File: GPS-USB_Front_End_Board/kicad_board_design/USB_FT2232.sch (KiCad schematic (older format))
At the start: 38 parts, among them J1 Micro-USB Connector, U1 93LCxxB, U2 FT2232HL-REEL, U3 L4931 LDO, Y1 12MHz Crystal

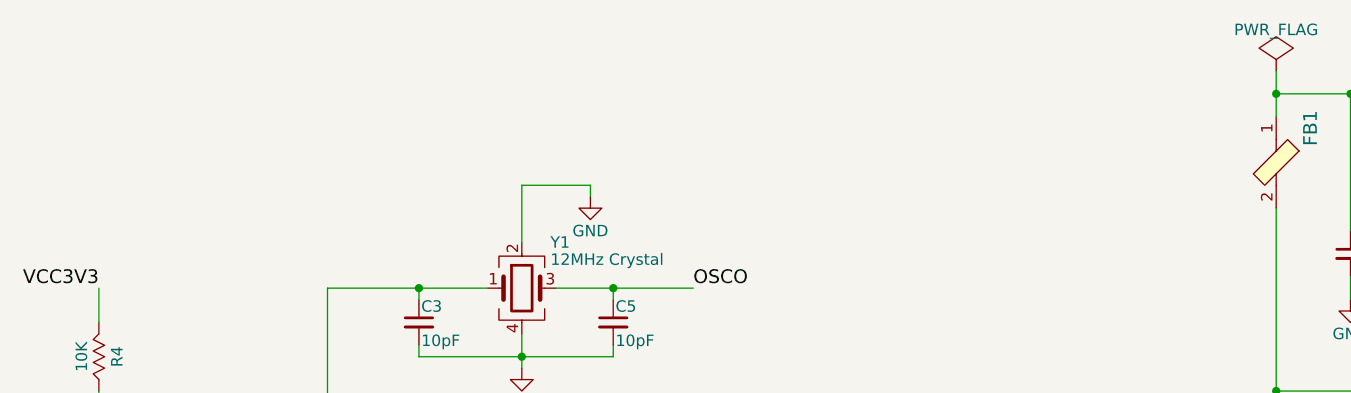
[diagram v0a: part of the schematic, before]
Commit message: Add more decoupling caps to 2232H.
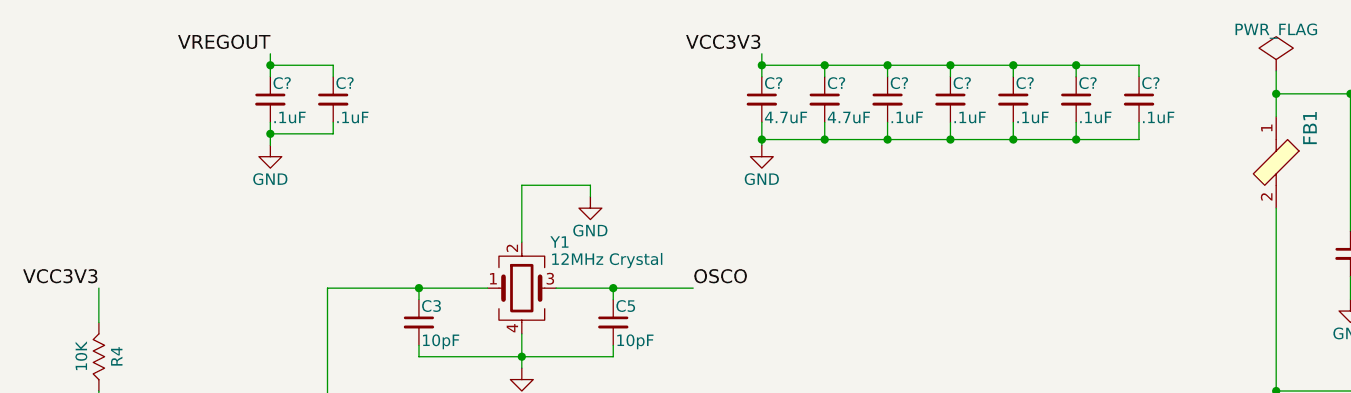
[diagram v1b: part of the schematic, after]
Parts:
- added C? (x2): 4.7uF, Capacitors_SMD:C_0402, symbol C_Small
- added C? (x7): .1uF, Capacitors_SMD:C_0402, symbol C_Small
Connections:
- net GND: now also C?.2, C?.2, C?.2, C?.2, C?.2, C?.2, C?.2, C?.2, C?.2
- net VCC3V3: now also C?.1, C?.1, C?.1, C?.1, C?.1, C?.1, C?.1
- net VREGOUT: now also C?.1, C?.1

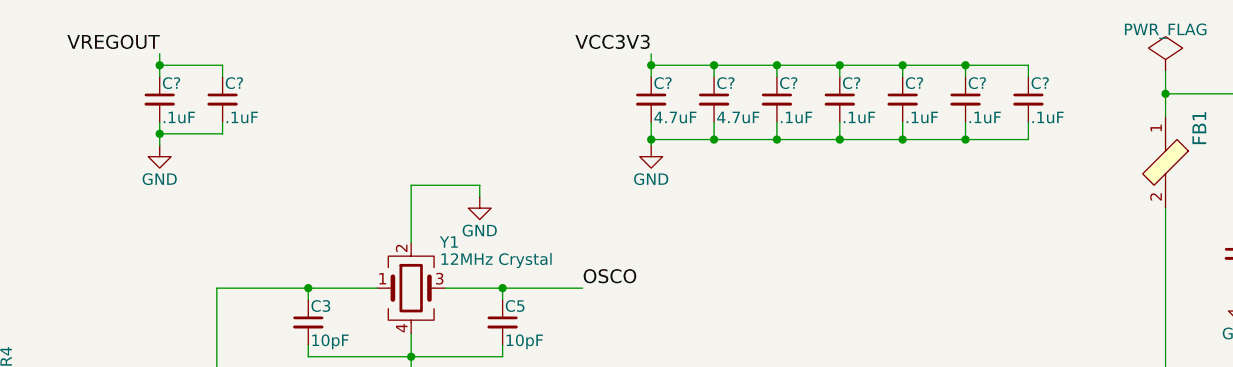
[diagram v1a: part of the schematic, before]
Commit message: Run DRC, generate and import netlist w/ new caps.
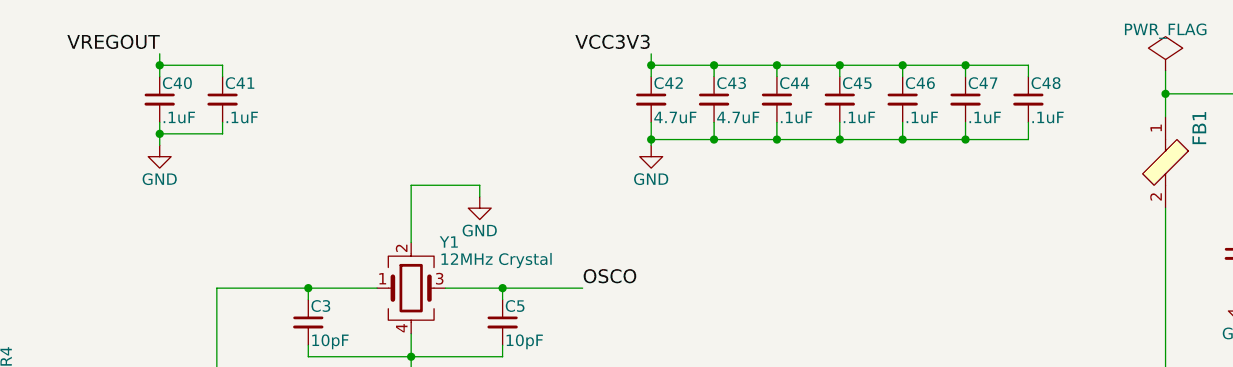
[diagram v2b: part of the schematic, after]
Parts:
- gave numbers to parts that had none: 9
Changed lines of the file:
@@
 VREGOUT
 $Comp
-L GND #PWR?
+L GND #PWR023
 U 1 1 5DB9B29B
 P 5050 1125
-F 0 "#PWR?" H 5050 875 50  0001 C CNN
+F 0 "#PWR023" H 5050 875 50  0001 C CNN
 F 1 "GND" H 5050 975 50  0000 C CNN
 F 2 "" H 5050 1125 50  0000 C CNN
@@
 $EndComp
 $Comp
-L GND #PWR?
+L GND #PWR024
 U 1 1 5DB9B3E6
 P 2900 1125
-F 0 "#PWR?" H 2900 875 50  0001 C CNN
+F 0 "#PWR024" H 2900 875 50  0001 C CNN
 F 1 "GND" H 2900 975 50  0000 C CNN
 F 2 "" H 2900 1125 50  0000 C CNN
@@
 $EndComp
 $Comp
-L C_Small C?
+L C_Small C42
 U 1 1 5DB9B46E
 P 5050 925
-F 0 "C?" H 5060 995 50  0000 L CNN
+F 0 "C42" H 5060 995 50  0000 L CNN
 F 1 "4.7uF" H 5060 845 50  0000 L CNN
 F 2 "Capacitors_SMD:C_0402" H 5050 925 50  0001 C CNN
@@
 $EndComp
 $Comp
-L C_Small C?
+L C_Small C44
 U 1 1 5DB9B73F
 P 5600 925
-F 0 "C?" H 5610 995 50  0000 L CNN
+F 0 "C44" H 5610 995 50  0000 L CNN
 F 1 ".1uF" H 5610 845 50  0000 L CNN
 F 2 "Capacitors_SMD:C_0402" H 5600 925 50  0001 C CNN
@@
 $EndComp
 $Comp
-L C_Small C?
+L C_Small C45
 U 1 1 5DB9B870
 P 5875 925
-F 0 "C?" H 5885 995 50  0000 L CNN
+F 0 "C45" H 5885 995 50  0000 L CNN
 F 1 ".1uF" H 5885 845 50  0000 L CNN
 F 2 "Capacitors_SMD:C_0402" H 5875 925 50  0001 C CNN
@@
 $EndComp
 $Comp
-L C_Small C?
+L C_Small C46
 U 1 1 5DB9B924
 P 6150 925
-F 0 "C?" H 6160 995 50  0000 L CNN
+F 0 "C46" H 6160 995 50  0000 L CNN
 F 1 ".1uF" H 6160 845 50  0000 L CNN
 F 2 "Capacitors_SMD:C_0402" H 6150 925 50  0001 C CNN
@@
 $EndComp
 $Comp
-L C_Small C?
+L C_Small C47
 U 1 1 5DB9BA31
 P 6425 925
-F 0 "C?" H 6435 995 50  0000 L CNN
+F 0 "C47" H 6435 995 50  0000 L CNN
 F 1 ".1uF" H 6435 845 50  0000 L CNN
 F 2 "Capacitors_SMD:C_0402" H 6425 925 50  0001 C CNN
@@
 $EndComp
 $Comp
-L C_Small C?
+L C_Small C48
 U 1 1 5DB9BAEB
 P 6700 925
-F 0 "C?" H 6710 995 50  0000 L CNN
+F 0 "C48" H 6710 995 50  0000 L CNN
 F 1 ".1uF" H 6710 845 50  0000 L CNN
 F 2 "Capacitors_SMD:C_0402" H 6700 925 50  0001 C CNN
@@
 $EndComp
 $Comp
-L C_Small C?
+L C_Small C40
 U 1 1 5DB9BBB0
 P 2900 925
-F 0 "C?" H 2910 995 50  0000 L CNN
+F 0 "C40" H 2910 995 50  0000 L CNN
 F 1 ".1uF" H 2910 845 50  0000 L CNN
 F 2 "Capacitors_SMD:C_0402" H 2900 925 50  0001 C CNN
@@
 $EndComp
 $Comp
-L C_Small C?
+L C_Small C41
 U 1 1 5DB9BCF8
 P 3175 925
-F 0 "C?" H 3185 995 50  0000 L CNN
+F 0 "C41" H 3185 995 50  0000 L CNN
 F 1 ".1uF" H 3185 845 50  0000 L CNN
 F 2 "Capacitors_SMD:C_0402" H 3175 925 50  0001 C CNN
@@
 Connection ~ 6425 1100
 $Comp
-L C_Small C?
+L C_Small C43
 U 1 1 5DB9EAF8
 P 5325 925
-F 0 "C?" H 5335 995 50  0000 L CNN
+F 0 "C43" H 5335 995 50  0000 L CNN
 F 1 "4.7uF" H 5335 845 50  0000 L CNN
 F 2 "Capacitors_SMD:C_0402" H 5325 925 50  0001 C CNN

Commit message: Partially laid out; ready to move some parts.
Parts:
- C34, C4: footprint Capacitors_SMD:C_0805_HandSoldering -> Capacitors_SMD:C_0402; MPN C2012X7R1C335K125AB -> C1005X5R0J335K050BC; SPN 445-7582-1-ND -> 445-5946-1-ND
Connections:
- net VCC3V3: no longer C48.1
- net VREGOUT: now also C48.1
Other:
- moved on the sheet: C48
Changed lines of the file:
@@
 F 0 "C4" H 3710 2970 50  0000 L CNN
 F 1 "3.3uF" H 3710 2820 50  0000 L CNN
-F 2 "Capacitors_SMD:C_0805_HandSoldering" H 3700 2900 50  0001 C CNN
+F 2 "Capacitors_SMD:C_0402" H 3700 2900 50  0001 C CNN
 F 3 "" H 3700 2900 50  0001 C CNN
 F 4 "TDK" H 0   0   50  0001 C CNN "MFR"
-F 5 "C2012X7R1C335K125AB" H 0   0   50  0001 C CNN "MPN"
+F 5 "C1005X5R0J335K050BC" H 0   0   50  0001 C CNN "MPN"
 F 6 "Digikey" H 0   0   50  0001 C CNN "SPR"
-F 7 "445-7582-1-ND" H 0   0   50  0001 C CNN "SPN"
+F 7 "445-5946-1-ND" H 0   0   50  0001 C CNN "SPN"
 F 8 "-" H 0   0   50  0001 C CNN "SPURL"
 	1    3700 2900
@@
 F 3 "" H 3350 3000 50  0000 C CNN
 	1    3350 3000
-	1    0    0    -1
-$EndComp
-$Comp
-L C_Small C34
-U 1 1 5B46F2DD
-P 5450 2700
-F 0 "C34" H 5460 2770 50  0000 L CNN
-F 1 "3.3uF" H 5460 2620 50  0000 L CNN
-F 2 "Capacitors_SMD:C_0805_HandSoldering" H 5450 2700 50  0001 C CNN
-F 3 "" H 5450 2700 50  0001 C CNN
-F 4 "TDK" H 0   0   50  0001 C CNN "MFR"
-F 5 "C2012X7R1C335K125AB" H 0   0   50  0001 C CNN "MPN"
-F 6 "Digikey" H 0   0   50  0001 C CNN "SPR"
-F 7 "445-7582-1-ND" H 0   0   50  0001 C CNN "SPN"
-F 8 "-" H 0   0   50  0001 C CNN "SPURL"
-	1    5450 2700
 	1    0    0    -1
 $EndComp
@@
 L C_Small C48
 U 1 1 5DB9BAEB
-P 6700 925
-F 0 "C48" H 6710 995 50  0000 L CNN
-F 1 ".1uF" H 6710 845 50  0000 L CNN
-F 2 "Capacitors_SMD:C_0402" H 6700 925 50  0001 C CNN
-F 3 "" H 6700 925 50  0001 C CNN
-F 4 "TDK" H -1000 -675 50  0001 C CNN "MFR"
-F 5 "CGA2B1X7R1C104K050BC" H -1000 -675 50  0001 C CNN "MPN"
-F 6 "Digikey" H -1000 -675 50  0001 C CNN "SPR"
-F 7 "445-5613-1-ND" H -1000 -675 50  0001 C CNN "SPN"
-F 8 "-" H -1000 -675 50  0001 C CNN "SPURL"
-	1    6700 925
+P 3450 925
+F 0 "C48" H 3460 995 50  0000 L CNN
+F 1 ".1uF" H 3460 845 50  0000 L CNN
+F 2 "Capacitors_SMD:C_0402" H 3450 925 50  0001 C CNN
+F 3 "" H 3450 925 50  0001 C CNN
+F 4 "TDK" H -4250 -675 50  0001 C CNN "MFR"
+F 5 "CGA2B1X7R1C104K050BC" H -4250 -675 50  0001 C CNN "MPN"
+F 6 "Digikey" H -4250 -675 50  0001 C CNN "SPR"
+F 7 "445-5613-1-ND" H -4250 -675 50  0001 C CNN "SPN"
+F 8 "-" H -4250 -675 50  0001 C CNN "SPURL"
+	1    3450 925
 	1    0    0    -1
 $EndComp
@@
 	2900 725  2900 825
 Wire Wire Line
-	2900 775  3175 775
+	2900 775  3450 775
 Wire Wire Line
 	3175 775  3175 825
@@
 	3175 1025 3175 1075
 Wire Wire Line
-	3175 1075 2900 1075
+	2900 1075 3450 1075
 Wire Wire Line
 	2900 1025 2900 1125
@@
 Wire Wire Line
 	5050 775  6700 775
-Wire Wire Line
-	6700 775  6700 825
 Connection ~ 5050 775
 Wire Wire Line
@@
 Connection ~ 5325 775
 Wire Wire Line
-	6700 1025 6700 1100
-Wire Wire Line
-	6700 1100 5050 1100
+	5050 1100 6700 1100
 Wire Wire Line
 	5050 1025 5050 1125
@@
 	1    0    0    -1
 $EndComp
+Wire Wire Line
+	3450 1075 3450 1025
+Connection ~ 3175 1075
+Wire Wire Line
+	3450 775  3450 825
+Connection ~ 3175 775
+$Comp
+L C_Small C34
+U 1 1 5DBA5421
+P 5450 2700
+F 0 "C34" H 5460 2770 50  0000 L CNN
+F 1 "3.3uF" H 5460 2620 50  0000 L CNN
+F 2 "Capacitors_SMD:C_0402" H 5450 2700 50  0001 C CNN
+F 3 "" H 5450 2700 50  0001 C CNN
+F 4 "TDK" H 1750 -200 50  0001 C CNN "MFR"
+F 5 "C1005X5R0J335K050BC" H 1750 -200 50  0001 C CNN "MPN"
+F 6 "Digikey" H 1750 -200 50  0001 C CNN "SPR"
+F 7 "445-5946-1-ND" H 1750 -200 50  0001 C CNN "SPN"
+F 8 "-" H 1750 -200 50  0001 C CNN "SPURL"
+	1    5450 2700
+	1    0    0    -1
+$EndComp

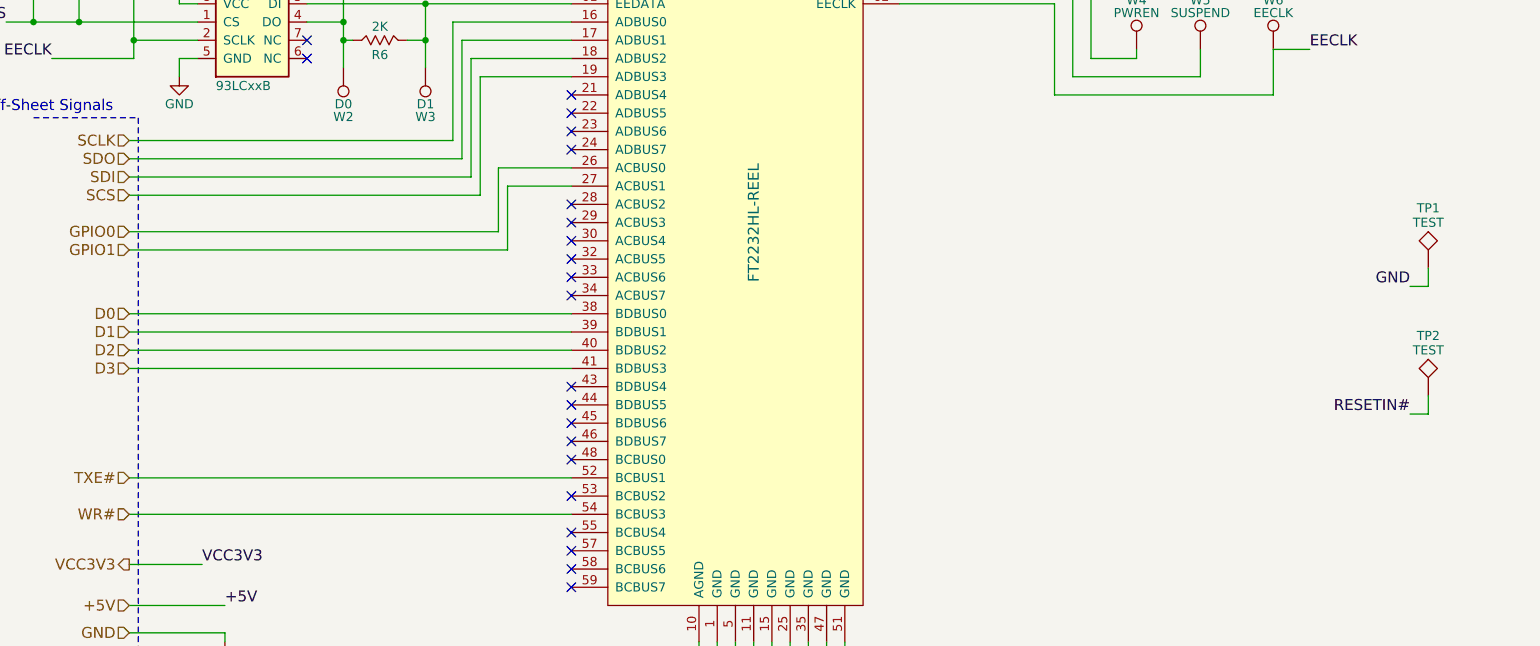
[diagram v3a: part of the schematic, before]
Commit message: Moved optional Maxim clk fix circuit to FTDI side.
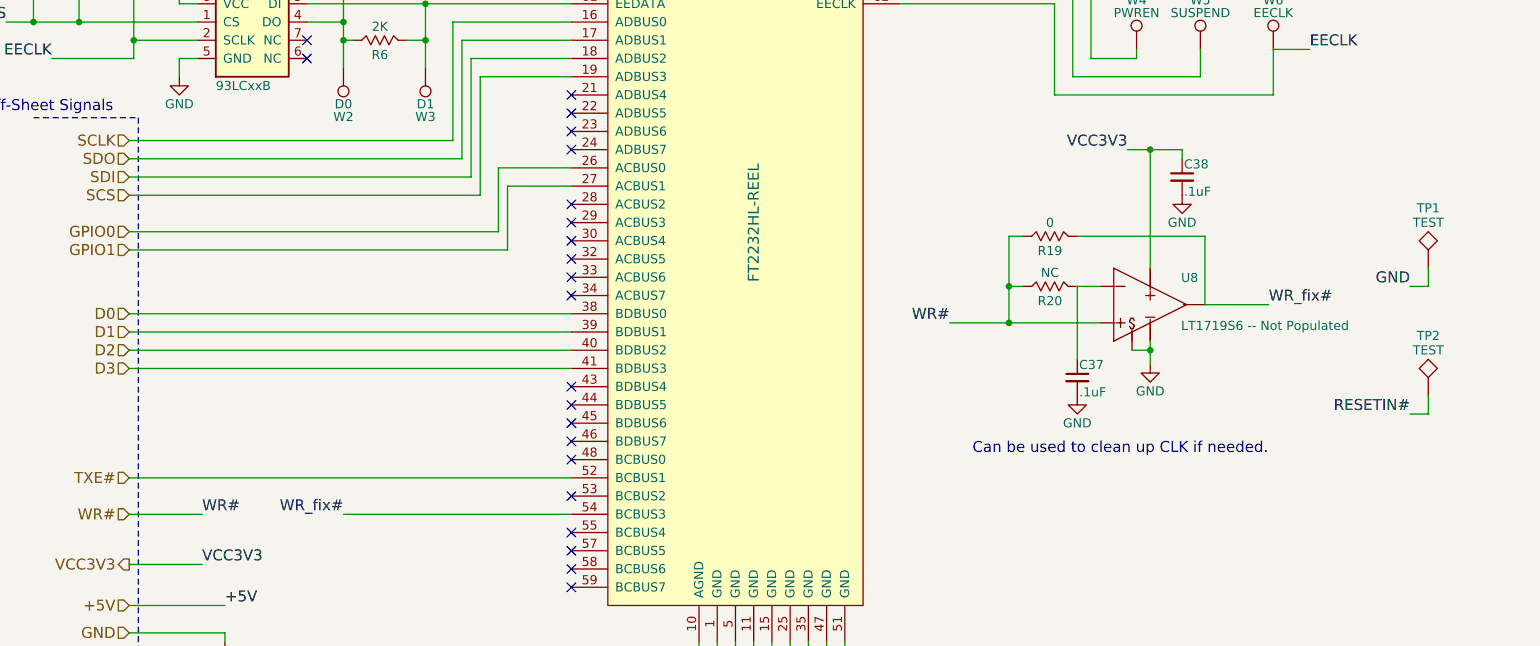
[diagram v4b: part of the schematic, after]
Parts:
- added C37, C38: .1uF, Capacitors_SMD:C_0402, symbol C_Small
- added R19: 0, Resistors_SMD:R_0603_HandSoldering, symbol R
- added R20: NC, Resistors_SMD:R_0603_HandSoldering, symbol R
- added U8: LT1719S6 -- Not Populated, rf:TSOT-23_S6, symbol LT1719S6
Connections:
- net GND: now also C37.2, C38.2, U8.2 (V-), U8.6 (SHDN)
- net VCC3V3: now also C38.1, U8.4 (V+)
- net WR#: now also R19.2, R20.2, U8.3 (IN+); no longer U2.54 (BCBUS3)
- new net: C37.1, R20.1, U8.1 (IN)
- new net WR_fix#: R19.1, U2.54 (BCBUS3), U8.5 (OUT)
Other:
- note added: "Can be used to clean up CLK if needed."
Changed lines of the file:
@@
 	1425 6500 3850 6500
-Wire Wire Line
-	3850 6700 1425 6700
 Wire Wire Line
 	1425 4650 3200 4650
@@
 	1    0    0    -1
 $EndComp
+$Comp
+L LT1719S6 U?
+U 1 1 5DBBDC28
+P 7025 5150
+AR Path="/5B22247E/5DBBDC28" Ref="U?"  Part="1"
+AR Path="/5B1BC185/5DBBDC28" Ref="U8"  Part="1"
+F 0 "U8" H 7194 4868 50  0000 L BNN
+F 1 "LT1719S6 -- Not Populated" H 7194 4605 50  0000 L BNN
+F 2 "rf:TSOT-23_S6" H 7025 5150 60  0001 C CNN
+F 3 "Unavailable" H 7025 5150 50  0001 L BNN
+F 4 "LT1719" H 7025 5150 50  0001 L BNN "Field4"
+F 5 "None" H 7025 5150 50  0001 L BNN "Field5"
+F 6 "Analog Devices / Linear Technology" H 7025 5150 50  0001 L BNN "Field6"
+F 7 "None" H 7025 5150 50  0001 L BNN "Field7"
+F 8 "Linear Tech" H -2350 3900 50  0001 C CNN "MFR"
+F 9 "LT1719IS6#TRMPBF" H -2350 3900 50  0001 C CNN "MPN"
+F 10 "Digikey" H -2350 3900 50  0001 C CNN "SPR"
+F 11 "LT1719IS6#TRMPBFCT-ND" H -2350 3900 50  0001 C CNN "SPN"
+F 12 "-" H -2350 3900 50  0001 C CNN "SPURL"
+	1    7025 5150
+	1    0    0    -1
+$EndComp
+$Comp
+L R R20
+U 1 1 5DBBDC34
+P 6475 5450
+F 0 "R20" V 6555 5450 50  0000 C CNN
+F 1 "NC" V 6400 5450 50  0000 C CNN
+F 2 "Resistors_SMD:R_0603_HandSoldering" V 6330 5450 50  0001 C CNN
+F 3 "" H 6400 5450 50  0001 C CNN
+F 4 "Vishay" H -2350 3900 50  0001 C CNN "MFR"
+F 5 "CRCW06030000Z0EBC" H -2350 3900 50  0001 C CNN "MPN"
+F 6 "Digikey" H -2350 3900 50  0001 C CNN "SPR"
+F 7 "541-4013-1-ND" H -2350 3900 50  0001 C CNN "SPN"
+F 8 "-" H -2350 3900 50  0001 C CNN "SPURL"
+	1    6475 5450
+	0    1    1    0
+$EndComp
+$Comp
+L GND #PWR?
+U 1 1 5DBBDC3B
+P 6625 6050
+F 0 "#PWR?" H 6625 5800 50  0001 C CNN
+F 1 "GND" H 6625 5900 50  0000 C CNN
+F 2 "" H 6625 6050 50  0000 C CNN
+F 3 "" H 6625 6050 50  0000 C CNN
+	1    6625 6050
+	1    0    0    -1
+$EndComp
+$Comp
+L GND #PWR?
+U 1 1 5DBBDC41
+P 7025 5875
+F 0 "#PWR?" H 7025 5625 50  0001 C CNN
+F 1 "GND" H 7025 5725 50  0000 C CNN
+F 2 "" H 7025 5875 50  0000 C CNN
+F 3 "" H 7025 5875 50  0000 C CNN
+	1    7025 5875
+	1    0    0    -1
+$EndComp
+$Comp
+L R R19
+U 1 1 5DBBDC4C
+P 6475 5175
+F 0 "R19" V 6555 5175 50  0000 C CNN
+F 1 "0" V 6400 5175 50  0000 C CNN
+F 2 "Resistors_SMD:R_0603_HandSoldering" V 6330 5175 50  0001 C CNN
+F 3 "" H 6400 5175 50  0001 C CNN
+F 4 "Vishay" H -2350 3900 50  0001 C CNN "MFR"
+F 5 "CRCW06030000Z0EBC" H -2350 3900 50  0001 C CNN "MPN"
+F 6 "Digikey" H -2350 3900 50  0001 C CNN "SPR"
+F 7 "541-4013-1-ND" H -2350 3900 50  0001 C CNN "SPN"
+F 8 "-" H -2350 3900 50  0001 C CNN "SPURL"
+	1    6475 5175
+	0    1    1    0
+$EndComp
+$Comp
+L C_Small C38
+U 1 1 5DBBDC58
+P 7200 4850
+F 0 "C38" H 7210 4920 50  0000 L CNN
+F 1 ".1uF" H 7210 4770 50  0000 L CNN
+F 2 "Capacitors_SMD:C_0402" H 7200 4850 50  0001 C CNN
+F 3 "" H 7200 4850 50  0001 C CNN
+F 4 "TDK" H -2350 3900 50  0001 C CNN "MFR"
+F 5 "CGA2B1X7R1C104K050BC" H -2350 3900 50  0001 C CNN "MPN"
+F 6 "Digikey" H -2350 3900 50  0001 C CNN "SPR"
+F 7 "445-5613-1-ND" H -2350 3900 50  0001 C CNN "SPN"
+F 8 "-" H -2350 3900 50  0001 C CNN "SPURL"
+	1    7200 4850
+	1    0    0    -1
+$EndComp
+$Comp
+L GND #PWR?
+U 1 1 5DBBDC5F
+P 7200 4950
+F 0 "#PWR?" H 7200 4700 50  0001 C CNN
+F 1 "GND" H 7200 4800 50  0000 C CNN
+F 2 "" H 7200 4950 50  0000 C CNN
+F 3 "" H 7200 4950 50  0000 C CNN
+	1    7200 4950
+	1    0    0    -1
+$EndComp
+Text Label 6900 4700 2    60   ~ 0
+VCC3V3
+Wire Wire Line
+	5925 5650 6750 5650
+Wire Wire Line
+	6750 5450 6625 5450
+Wire Wire Line
+	6325 5450 6250 5450
+Wire Wire Line
+	6250 5175 6250 5650
+Wire Wire Line
+	6625 5450 6625 5850
+Wire Wire Line
+	7025 5750 7025 5875
+Wire Wire Line
+	6925 5800 7025 5800
+Wire Wire Line
+	6250 5175 6325 5175
+Wire Wire Line
+	6625 5175 7325 5175
+Wire Wire Line
+	7325 5175 7325 5550
+Wire Wire Line
+	7325 5550 7675 5550
+Wire Wire Line
+	6900 4700 7200 4700
+Wire Wire Line
+	7025 4700 7025 5350
+Wire Wire Line
+	7200 4700 7200 4750
+Connection ~ 6250 5650
+Connection ~ 7025 5800
+Connection ~ 6250 5450
+Connection ~ 7025 4700
+$Comp
+L C_Small C37
+U 1 1 5DBBDC7D
+P 6625 5950
+F 0 "C37" H 6635 6020 50  0000 L CNN
+F 1 ".1uF" H 6635 5870 50  0000 L CNN
+F 2 "Capacitors_SMD:C_0402" H 6625 5950 50  0001 C CNN
+F 3 "" H 6625 5950 50  0001 C CNN
+F 4 "TDK" H 1700 4050 50  0001 C CNN "MFR"
+F 5 "CGA2B1X7R1C104K050BC" H 1700 4050 50  0001 C CNN "MPN"
+F 6 "Digikey" H 1700 4050 50  0001 C CNN "SPR"
+F 7 "445-5613-1-ND" H 1700 4050 50  0001 C CNN "SPN"
+F 8 "-" H 1700 4050 50  0001 C CNN "SPURL"
+	1    6625 5950
+	1    0    0    -1
+$EndComp
+Text Label 1825 6700 0    60   ~ 0
+WR#
+Text Label 5925 5650 2    60   ~ 0
+WR#
+Text Label 7675 5550 0    60   ~ 0
+WR_fix#
+Text Label 2600 6700 2    60   ~ 0
+WR_fix#
+Wire Wire Line
+	1425 6700 1825 6700
+Wire Wire Line
+	2600 6700 3850 6700
+Text Notes 6050 6375 0    60   ~ 0
+Can be used to clean up CLK if needed.
 $EndSCHEMATC
